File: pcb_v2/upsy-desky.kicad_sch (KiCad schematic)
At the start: 62 parts, among them J1 RJ45, J2 RJ45, J3 USB_C_ReceptacleUSB2.0, J4 Conn_01x03_Socket, J5 Screw_Terminal_01x03, J6 Conn_01x03_Pin, Q3 2N7002, Q4 2N7002, Q5 2N7002, Q6 2N7002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

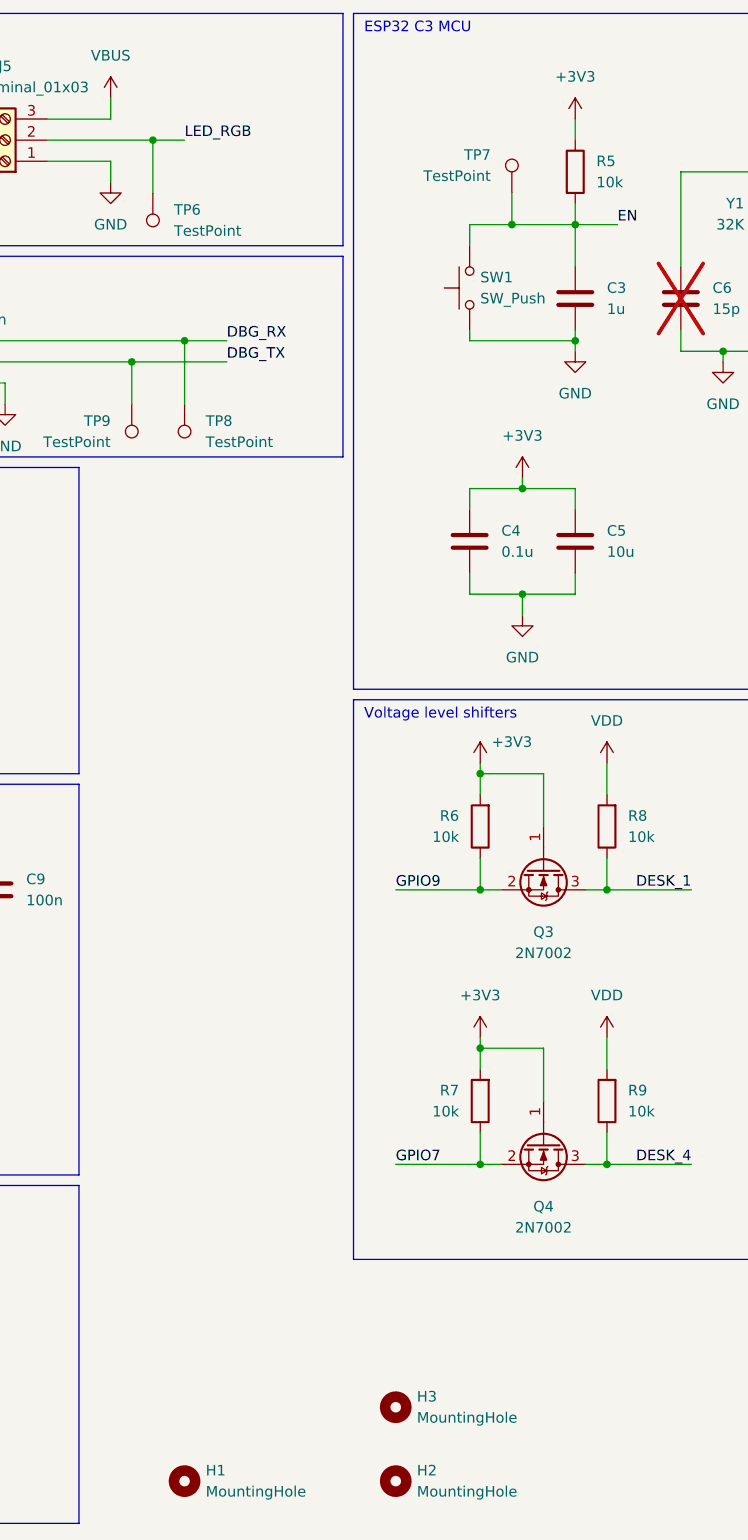
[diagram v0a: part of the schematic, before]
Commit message: Updated BOM for PCBWay
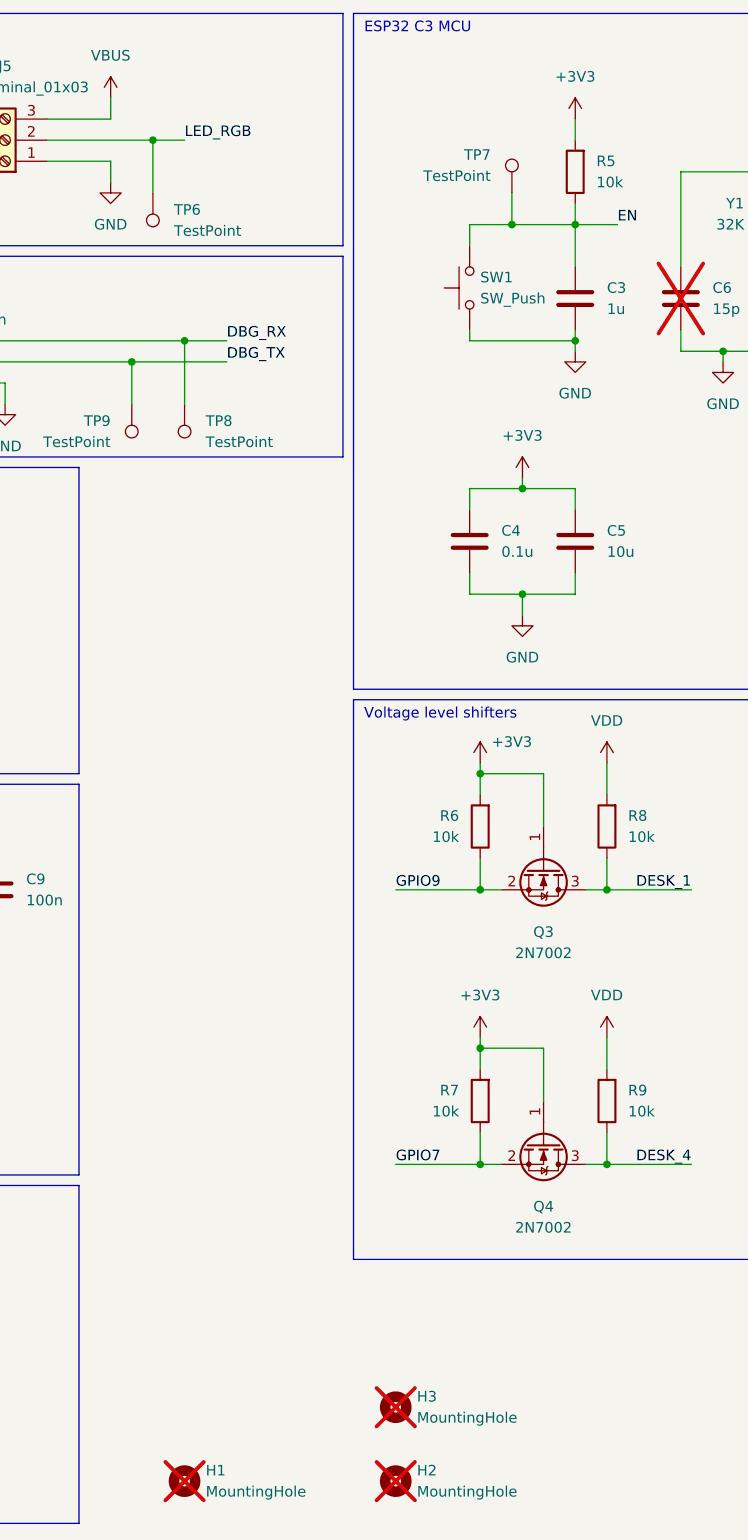
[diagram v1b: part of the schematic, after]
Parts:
- C1, C2, C5: DigiKey (none) -> 490-GRM155R60J106ME05JCT-ND; MANUFACTURER (none) -> Murata Electronics
- C3: Alt MPN (none) -> CL05A105KP5NNNC; DigiKey (none) -> 3372-0402W105K100HITR-ND; MANUFACTURER (none) -> Aillen
- C4: Alt MPN (none) -> GRM155R71H104KE14D; DigiKey (none) -> 3372-0402B104K160HITR-ND; MANUFACTURER (none) -> Aillen
- C6, C7: MPN (none) -> TCC0402COG150J500AT
- C8: DigiKey (none) -> 1276-1056-2-ND; MANUFACTURER (none) -> Samsung Electro-Mechanics; MPN (none) -> CL05A475MQ5NRNC
- C9: DigiKey (none) -> 311-1345-2-ND; MANUFACTURER (none) -> YAGEO; MPN (none) -> CC0402KRX7R6BB104
- D1: Alt MPN (none) -> B5817WS-TP; DigiKey (none) -> B5817WS-TPMSTR-ND; MANUFACTURER (none) -> Micro Commercial Co; MPN 1N5817 -> B5817WS-TP
- H1, H2, H3: now not fitted
- J1, J2: DigiKey (none) -> 54601-708LF-ND
- J4: DigiKey (none) -> WM4112-ND; MANUFACTURER (none) -> Molex; MPN (none) -> 0022272031
- J5: DigiKey (none) -> 1920-30.003-ND; MANUFACTURER (none) -> Altech; MPN (none) -> 30-003
- J6: DigiKey (none) -> 455-B3B-EH-A-ND; MANUFACTURER (none) -> JST Sales America Inc; MPN (none) -> B3B-EH-A
- Q3, Q4, Q5, Q6, Q7, Q8: DigiKey (none) -> 2N7002NTR-ND; MANUFACTURER (none) -> Onsemi
- R1, R2: DigiKey (none) -> 3372-CR0402JC5K1S01TR-ND; MANUFACTURER (none) -> Aillen; MPN RC0402JR-075R1L -> CR0402JC5K1S01
- R10, R11, R12, R13, R14, R15, R16, R17, R5, R6, R7, R8, R9: DigiKey (none) -> 13-RC0402JR-1310KLTR-ND; MANUFACTURER (none) -> YAGEO
- R19, R20: DigiKey (none) -> 13-RC0402JR-1310KLTR-ND; MANUFACTURER (none) -> YAGEO; MPN (none) -> RC0402JR-1310KL
- R3, R4: DigiKey (none) -> 311-2.20KLRTR-ND; MANUFACTURER (none) -> YAGEO; MPN (none) -> RC0402FR-072K2L
- SW1: DigiKey (none) -> 401-1428-2-ND; MANUFACTURER (none) -> C&K; MPN (none) -> KMR223GLFG
- U1: DigiKey (none) -> 497-16538-2-ND; MANUFACTURER (none) -> STMicroelectronics; MPN (none) -> VL53L0CXV0DH/1
- U2: DigiKey (none) -> 4518-AMS1117-3.3TR-ND; MANUFACTURER (none) -> Onsemi / AMS / UMW
- U4: DigiKey (none) -> 1965-ESP32-C3-WROOM-02-N4TR-ND; MANUFACTURER (none) -> Espressif Systems; MPN (none) -> ESP32-C3-WROOM-02-N4
- Y1: DigiKey (none) -> 887-1425-2-ND; MANUFACTURER (none) -> TXC CORPORATION; MPN (none) -> 9HT11-32-768KDZF-T
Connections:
- net +3V3: now also R5.2; no longer R5.1
- net EN: now also R5.1; no longer R5.2
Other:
- moved on the sheet: R5
